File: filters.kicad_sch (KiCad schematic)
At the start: 4 parts, among them U6 MCP6004

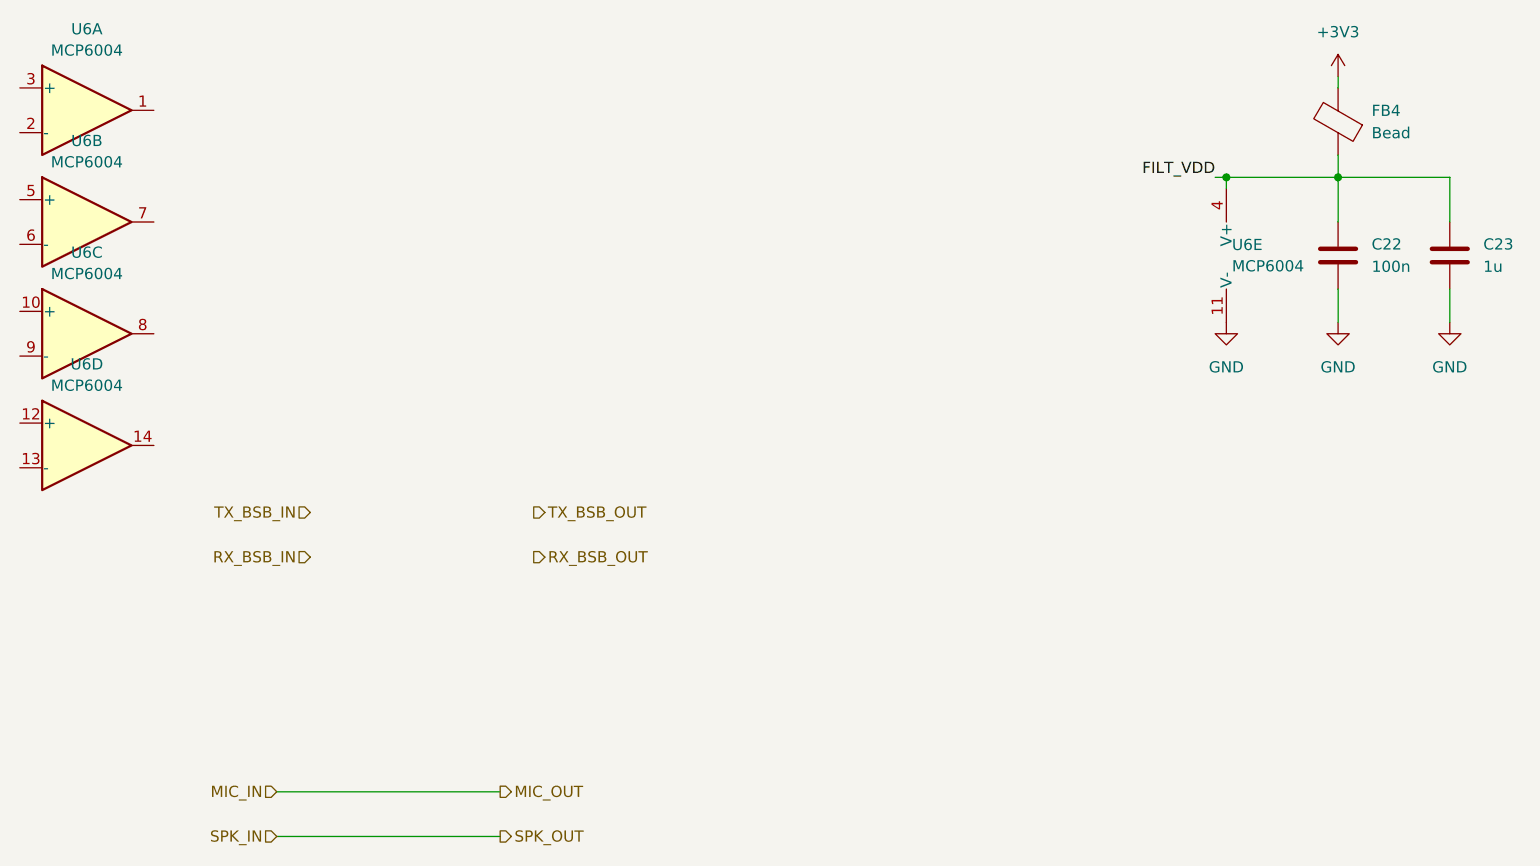
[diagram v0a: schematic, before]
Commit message: spk/mic update
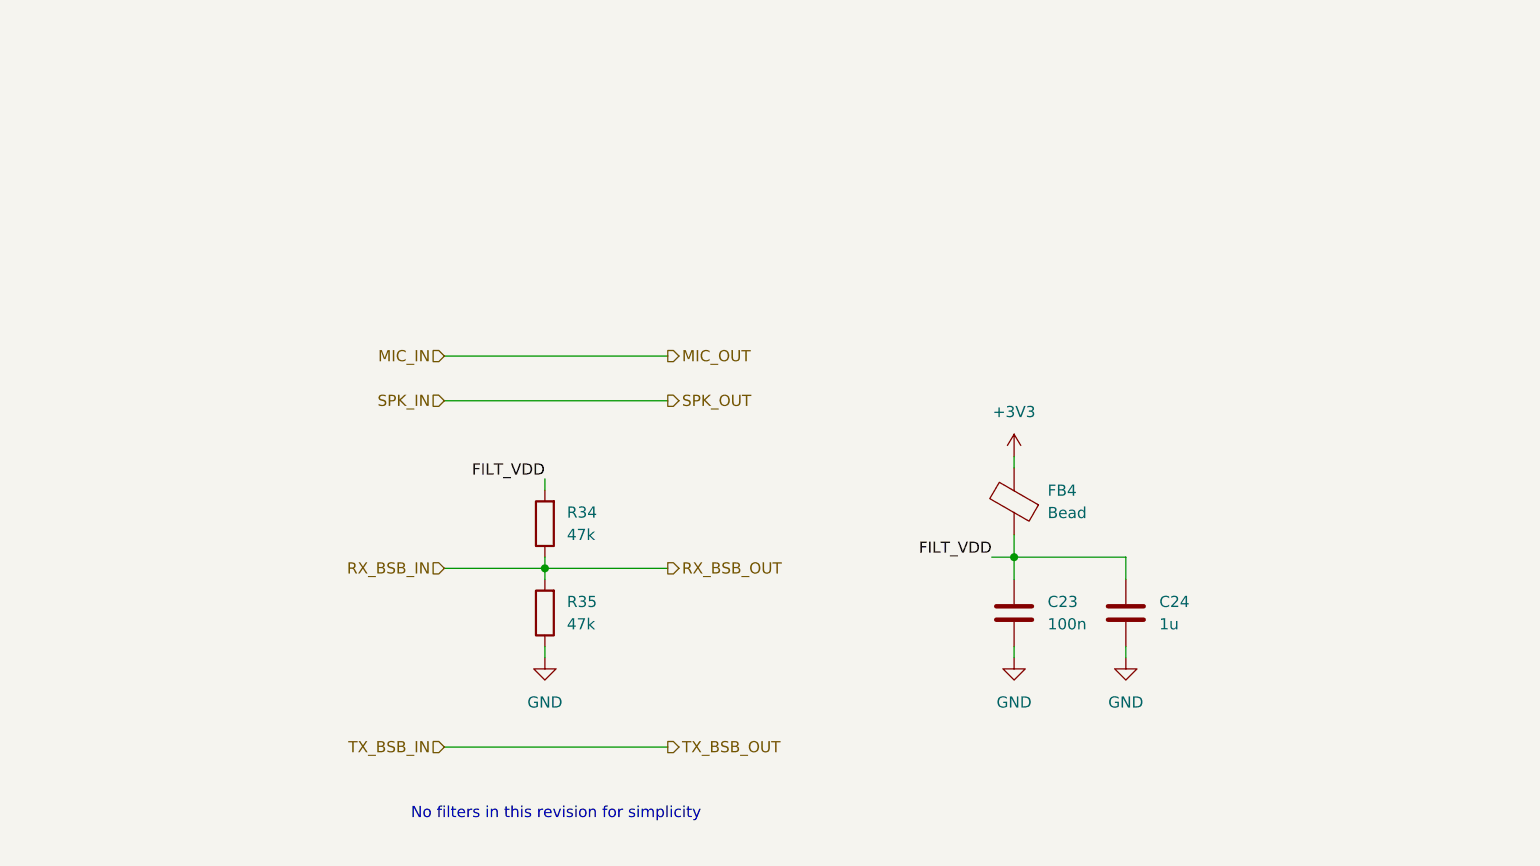
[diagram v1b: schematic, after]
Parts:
- removed U6: MCP6004, symbol Amplifier_Operational:MCP6004
- added R34, R35: 47k, Inductor_SMD:L_0805_2012Metric, symbol Device:R
- renumbered C22 to C23, C23 to C24
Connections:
- net FILT_VDD: now also R34.2
- net GND: now also R35.1
- net RX_BSB_IN: now also R34.1, R35.2
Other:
- note added: "No filters in this revision for simplicity"
- moved on the sheet: C23, C24, FB4

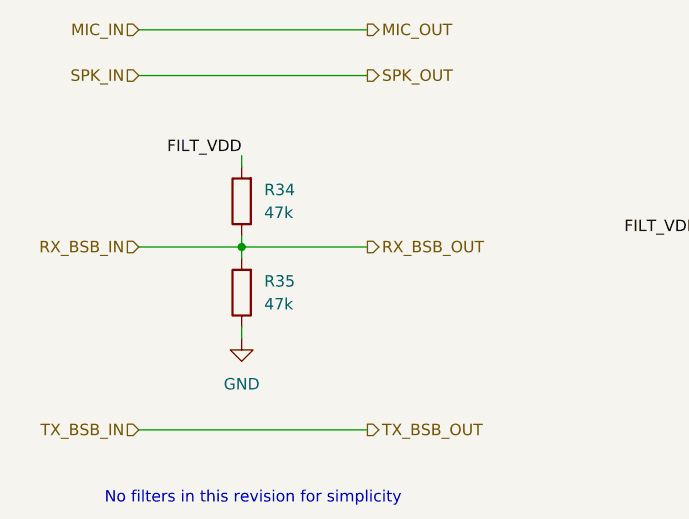
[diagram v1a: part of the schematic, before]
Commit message: removed audio part
- added buzzer
- added battery voltage measurement
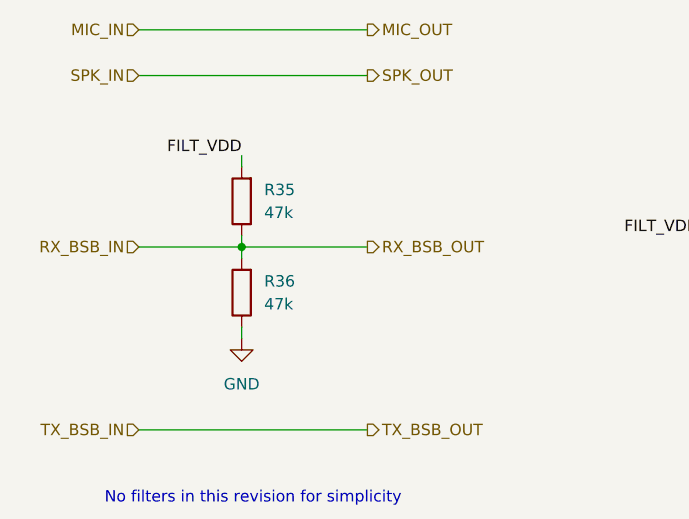
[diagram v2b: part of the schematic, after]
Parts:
- renumbered R34 to R35, R35 to R36
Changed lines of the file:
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@@
 	(title_block
 		(title "Mainboard replacement for Nokia 3310")
-		(date "28-10-2024")
+		(date "29-10-2024")
 		(rev "Rev A")
 		(company "M17 Project")
@@
 		(dnp no)
 		(fields_autoplaced yes)
-		(property "Reference" "#PWR066"
+		(property "Reference" "#PWR067"
 			(at 115.57 111.76 0)
 			(effects
@@
 			(project "M17_3310"
 				(path "/8d65c5ef-7a02-4454-aee5-ab9c49e4aeab/ed3b33e1-45d0-4aa4-a9fa-64f3530c7cd6"
-					(reference "#PWR066")
+					(reference "#PWR067")
 					(unit 1)
 				)
@@
 		(dnp no)
 		(fields_autoplaced yes)
-		(property "Reference" "R35"
+		(property "Reference" "R36"
 			(at 118.0704 99.0599 0)
 			(effects
@@
 			(project "M17_3310"
 				(path "/8d65c5ef-7a02-4454-aee5-ab9c49e4aeab/ed3b33e1-45d0-4aa4-a9fa-64f3530c7cd6"
-					(reference "R35")
+					(reference "R36")
 					(unit 1)
 				)
@@
 		(dnp no)
 		(fields_autoplaced yes)
-		(property "Reference" "#PWR068"
+		(property "Reference" "#PWR069"
 			(at 168.91 111.76 0)
 			(effects
@@
 			(project "M17_3310"
 				(path "/8d65c5ef-7a02-4454-aee5-ab9c49e4aeab/ed3b33e1-45d0-4aa4-a9fa-64f3530c7cd6"
-					(reference "#PWR068")
+					(reference "#PWR069")
 					(unit 1)
 				)
@@
 		(dnp no)
 		(fields_autoplaced yes)
-		(property "Reference" "#PWR067"
+		(property "Reference" "#PWR068"
 			(at 168.91 86.36 0)
 			(effects
@@
 			(project "M17_3310"
 				(path "/8d65c5ef-7a02-4454-aee5-ab9c49e4aeab/ed3b33e1-45d0-4aa4-a9fa-64f3530c7cd6"
-					(reference "#PWR067")
+					(reference "#PWR068")
 					(unit 1)
 				)
@@
 		(dnp no)
 		(fields_autoplaced yes)
-		(property "Reference" "#PWR069"
+		(property "Reference" "#PWR070"
 			(at 181.61 111.76 0)
 			(effects
@@
 			(project "M17_3310"
 				(path "/8d65c5ef-7a02-4454-aee5-ab9c49e4aeab/ed3b33e1-45d0-4aa4-a9fa-64f3530c7cd6"
-					(reference "#PWR069")
+					(reference "#PWR070")
 					(unit 1)
 				)
@@
 		(dnp no)
 		(fields_autoplaced yes)
-		(property "Reference" "R34"
+		(property "Reference" "R35"
 			(at 118.0704 88.8999 0)
 			(effects
@@
 			(project "M17_3310"
 				(path "/8d65c5ef-7a02-4454-aee5-ab9c49e4aeab/ed3b33e1-45d0-4aa4-a9fa-64f3530c7cd6"
-					(reference "R34")
+					(reference "R35")
 					(unit 1)
 				)
